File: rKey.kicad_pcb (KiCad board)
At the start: 2 copper layers, 54.4 x 78.7 mm, 35 parts, among them IC1 7805, J1 Conn_01x06, Q1 BC337, Q2 BC337, Q3 BC337, Q4 BC337, Q5 BC327, Q6 BC337, Q7 BC337, Q8 BC337, U1 TL084BCN, U2 TL084BCN

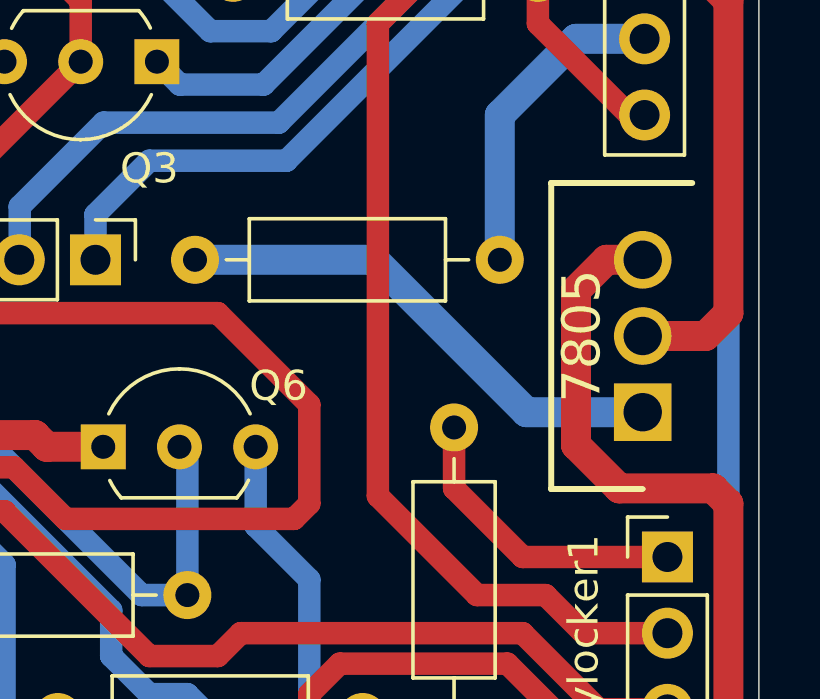
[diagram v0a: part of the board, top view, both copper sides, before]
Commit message: fix: 7805 wrong oriented
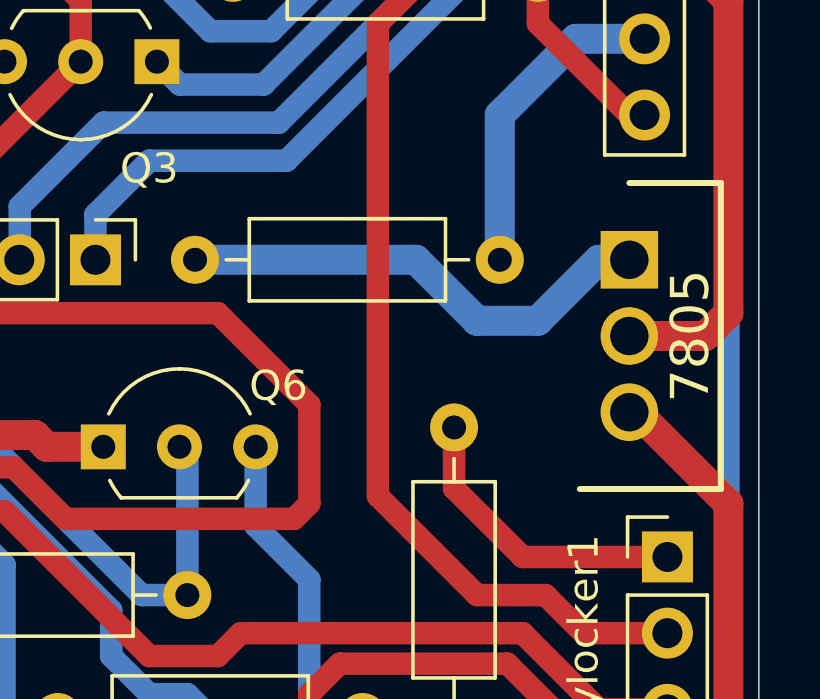
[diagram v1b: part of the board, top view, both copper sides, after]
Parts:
- moved IC1 5.10 mm to (165.1, 95.5), turned to -90 degrees
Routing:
- net Net-(C1-Pad1): track 48.4 -> 39.1 mm
- net Net-(IC1-Pad1): track 17.0 -> 16.2 mm
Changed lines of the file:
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@@
   )
   (footprint "KiCad:TO254P470X1000X1610-3P" (layer "F.Cu")
-    (at 165.546 100.584 90)
+    (at 165.1 95.504 -90)
     (descr "7805")
     (tags "Integrated Circuit")
@@
     (fp_line (start -2.56 -1.78) (end -1.29 -3.05) (layer "F.Fab") (width 0.1))
     (fp_line (start -2.56 -3.05) (end 7.64 -3.05) (layer "F.Fab") (width 0.1))
-    (pad "1" thru_hole rect locked (at 0 0 90) (size 1.92 1.92) (drill 1.28) (layers *.Cu *.Mask)
+    (pad "1" thru_hole rect locked (at 0 0 270) (size 1.92 1.92) (drill 1.28) (layers *.Cu *.Mask)
       (net 11 "Net-(IC1-Pad1)") (pinfunction "IN") (pintype "passive"))
-    (pad "2" thru_hole circle locked (at 2.54 0 90) (size 1.92 1.92) (drill 1.28) (layers *.Cu *.Mask)
+    (pad "2" thru_hole circle locked (at 2.54 0 270) (size 1.92 1.92) (drill 1.28) (layers *.Cu *.Mask)
       (net 4 "GND") (pinfunction "GND") (pintype "passive"))
-    (pad "3" thru_hole circle locked (at 5.08 0 90) (size 1.92 1.92) (drill 1.28) (layers *.Cu *.Mask)
+    (pad "3" thru_hole circle locked (at 5.08 0 270) (size 1.92 1.92) (drill 1.28) (layers *.Cu *.Mask)
       (net 43 "Net-(C1-Pad1)") (pinfunction "OUT") (pintype "passive"))
     (model "7805.stp"
@@
   (segment (start 137.145 95.504) (end 137.145 98.029) (width 0.75) (layer "B.Cu") (net 10))
   (segment (start 150.368 102.002) (end 150.368 106.68) (width 0.75) (layer "B.Cu") (net 10))
-  (segment (start 161.671 100.584) (end 165.546 100.584) (width 1) (layer "B.Cu") (net 11))
-  (segment (start 156.591 95.504) (end 161.671 100.584) (width 1) (layer "B.Cu") (net 11))
-  (segment (start 150.622 95.504) (end 156.591 95.504) (width 1) (layer "B.Cu") (net 11))
+  (segment (start 164.084 95.504) (end 165.1 95.504) (width 1) (layer "B.Cu") (net 11))
+  (segment (start 160.02 97.536) (end 162.052 97.536) (width 1) (layer "B.Cu") (net 11))
+  (segment (start 157.988 95.504) (end 160.02 97.536) (width 1) (layer "B.Cu") (net 11))
+  (segment (start 150.622 95.504) (end 157.988 95.504) (width 1) (layer "B.Cu") (net 11))
+  (segment (start 162.052 97.536) (end 164.084 95.504) (width 1) (layer "B.Cu") (net 11))
   (segment (start 160.782 90.678) (end 163.322 88.138) (width 1) (layer "B.Cu") (net 12))
   (segment (start 163.322 88.138) (end 165.608 88.138) (width 1) (layer "B.Cu") (net 12))
@@
   (segment (start 123.952 83.058) (end 124.714 82.296) (width 1) (layer "B.Cu") (net 41))
   (segment (start 124.714 82.296) (end 124.714 77.851) (width 1) (layer "B.Cu") (net 41))
-  (segment (start 164.338 95.504) (end 165.738405 95.504) (width 1) (layer "F.Cu") (net 43))
-  (segment (start 163.322 96.52) (end 164.338 95.504) (width 1) (layer "F.Cu") (net 43))
-  (segment (start 163.322 101.68) (end 163.322 96.52) (width 1) (layer "F.Cu") (net 43))
-  (segment (start 168.402 103.632) (end 167.894 103.124) (width 1) (layer "F.Cu") (net 43))
+  (segment (start 168.402 122.428) (end 168.402 103.632) (width 1) (layer "F.Cu") (net 43))
+  (segment (start 165.354 100.584) (end 165.1 100.584) (width 1) (layer "F.Cu") (net 43))
+  (segment (start 167.64 123.19) (end 168.402 122.428) (width 1) (layer "F.Cu") (net 43))
   (segment (start 166.37 123.19) (end 167.64 123.19) (width 1) (layer "F.Cu") (net 43))
-  (segment (start 167.894 103.124) (end 164.766 103.124) (width 1) (layer "F.Cu") (net 43))
-  (segment (start 168.402 122.428) (end 168.402 103.632) (width 1) (layer "F.Cu") (net 43))
-  (segment (start 167.64 123.19) (end 168.402 122.428) (width 1) (layer "F.Cu") (net 43))
-  (segment (start 164.766 103.124) (end 163.322 101.68) (width 1) (layer "F.Cu") (net 43))
+  (segment (start 168.402 103.632) (end 165.354 100.584) (width 1) (layer "F.Cu") (net 43))
   (segment (start 160.02 115.316) (end 161.036 116.332) (width 1) (layer "B.Cu") (net 43))
   (segment (start 164.084 123.19) (end 166.37 123.19) (width 1) (layer "B.Cu") (net 43))

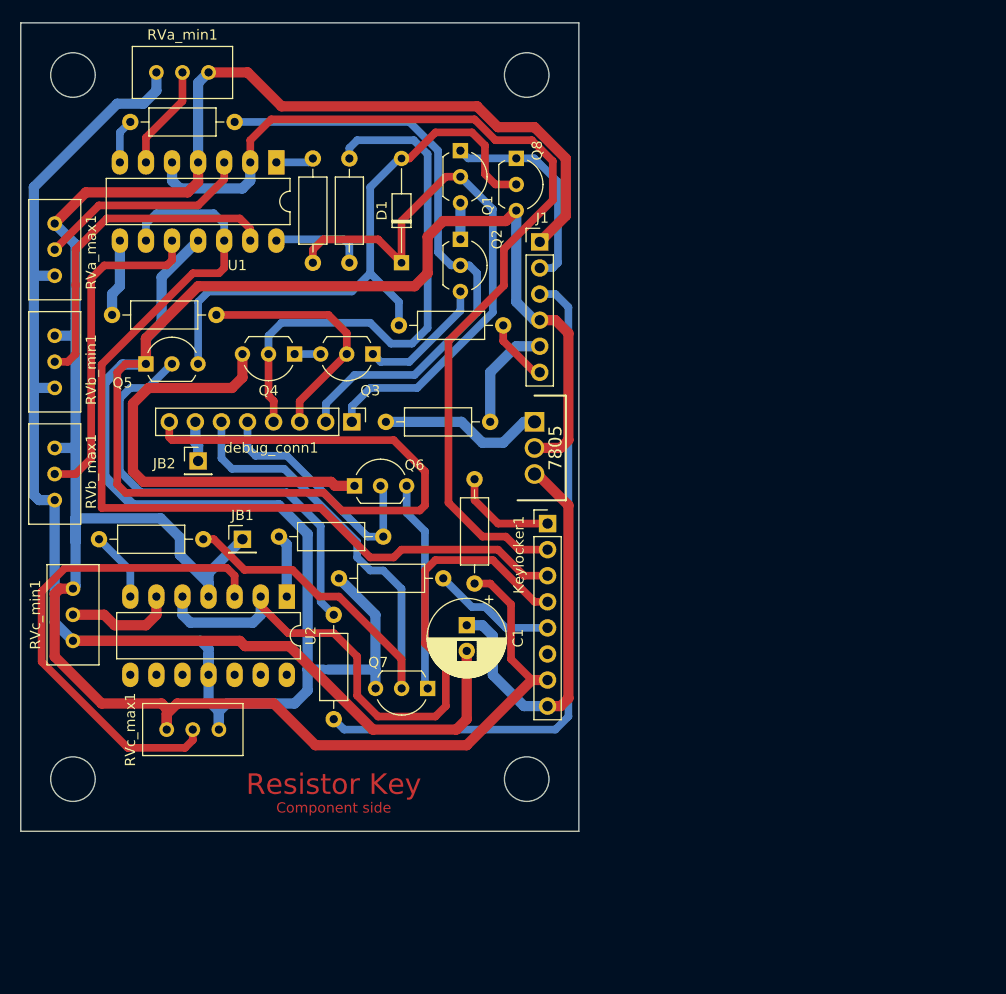
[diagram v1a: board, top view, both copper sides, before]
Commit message: fix: small changes in footprint associations
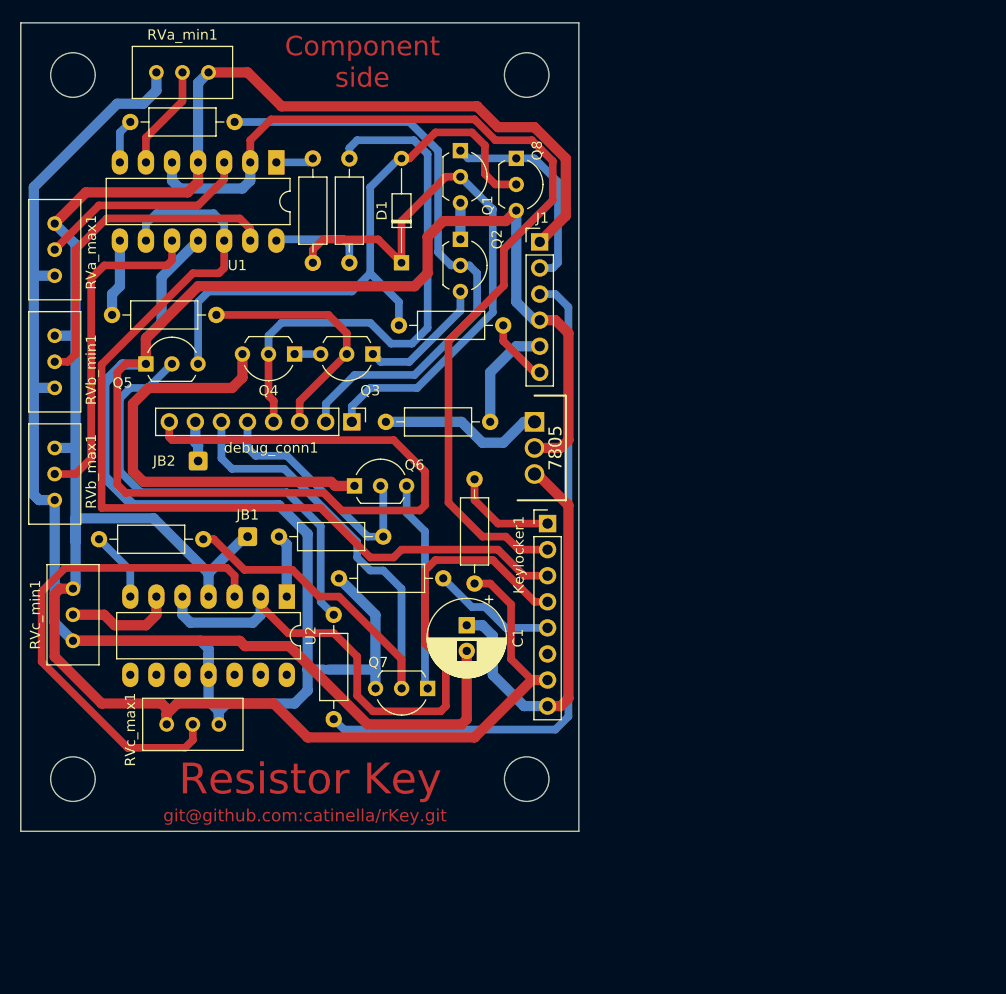
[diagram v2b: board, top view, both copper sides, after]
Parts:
- JB1, JB2: footprint Connector_PinHeader_2.54mm:PinHeader_1x01_P2.54mm_Vertical -> Connector_Wire:SolderWire-0.25sqmm_1x01_D0.65mm_OD1.7mm
- moved JB1 0.57 mm to (137.2, 106.7)
- moved RVc_max1 0.51 mm to (129.3, 125.0)
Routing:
- net Net-(J1-Pad1): track 219.9 -> 216.7 mm
- net GND: track 387.2 -> 385.7 mm
- net Net-(RVc_max1-Pad2): track 48.5 -> 49.0 mm
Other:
- board text added: "git@github.com:catinella/rKey.git"

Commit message: Preliminary version
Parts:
- removed JB1, JB2: Conn_01x01, Connector_Wire:SolderWire-0.25sqmm_1x01_D0.65mm_OD1.7mm
- added R11: 100K, Resistor_THT:R_Axial_DIN0207_L6.3mm_D2.5mm_P10.16mm_Horizontal, F.Cu at (128.8, 103.1)
- added R12: 100K, Resistor_THT:R_Axial_DIN0207_L6.3mm_D2.5mm_P10.16mm_Horizontal, F.Cu at (128.8, 106.4)
- added R14: 100K, Resistor_THT:R_Axial_DIN0207_L6.3mm_D2.5mm_P10.16mm_Horizontal, F.Cu at (128.8, 99.8)
- added R15: 100K, Resistor_THT:R_Axial_DIN0207_L6.3mm_D2.5mm_P10.16mm_Horizontal, F.Cu at (151.6, 99.8)
- added R16: 100K, Resistor_THT:R_Axial_DIN0207_L6.3mm_D2.5mm_P10.16mm_Horizontal, F.Cu at (151.6, 106.4)
- added R17: 100K, Resistor_THT:R_Axial_DIN0207_L6.3mm_D2.5mm_P10.16mm_Horizontal, F.Cu at (151.6, 103.1)
- moved C1 45.0 mm to (202.9, 108.1)
- moved R13 21.6 mm to (124.0, 114.0)
- moved R10 20.4 mm to (145.3, 128.0)
- moved RVc_max1 14.2 mm to (118.4, 115.8), turned to 90 degrees
- moved Q7 12.5 mm to (155.8, 109.0), turned to -90 degrees
- moved Q6 8.09 mm to (155.6, 101.3), turned to -90 degrees
- moved RVc_min1 7.82 mm to (118.4, 104.1)
- moved R8 6.76 mm to (128.3, 110.7)
- moved RVa_max1 5.32 mm to (118.4, 70.9)
- moved RVb_min1 5.32 mm to (118.4, 81.8)
- moved RVb_max1 5.08 mm to (118.4, 93.0)
- moved R7 5.00 mm to (142.2, 111.3)
- moved U2 4.20 mm to (142.7, 116.3)
- moved R1 2.87 mm to (161.3, 109.2)
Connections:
- debug_conn1 pad 7: Net-(JB2-Pad1) -> Net-(J1-Pad1)
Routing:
- net GND: track 385.7 -> 249.0 mm
- net Net-(Keylocker1-Pad3): track 91.0 -> 30.3 mm
- net Net-(Q6-Pad2): track 24.4 -> 52.0 mm
- net Net-(RVc_max1-Pad2): track 49.0 -> 23.9 mm
- net Net-(J1-Pad3): track 67.0 -> 43.2 mm
- net Net-(Keylocker1-Pad4): track 65.5 -> 42.2 mm
- net Net-(Q7-Pad2): track 64.0 -> 42.9 mm
- net Net-(Q4-Pad3): track 42.8 -> 63.0 mm
- net Net-(Q6-Pad3): track 20.6 -> 2.60 mm
- net Net-(Q3-Pad2): track 24.0 -> 40.9 mm
- net Net-(Q5-Pad2): track 44.5 -> 27.6 mm
- net Net-(Q4-Pad2): track 52.5 -> 68.9 mm
- net Net-(C1-Pad1): track 39.1 -> 23.4 mm
- net Net-(J1-Pad1): track 216.7 -> 231.1 mm
- net Net-(Keylocker1-Pad5): track 12.2 -> 0.00 mm
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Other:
- outline, holes or cut-outs redrawn

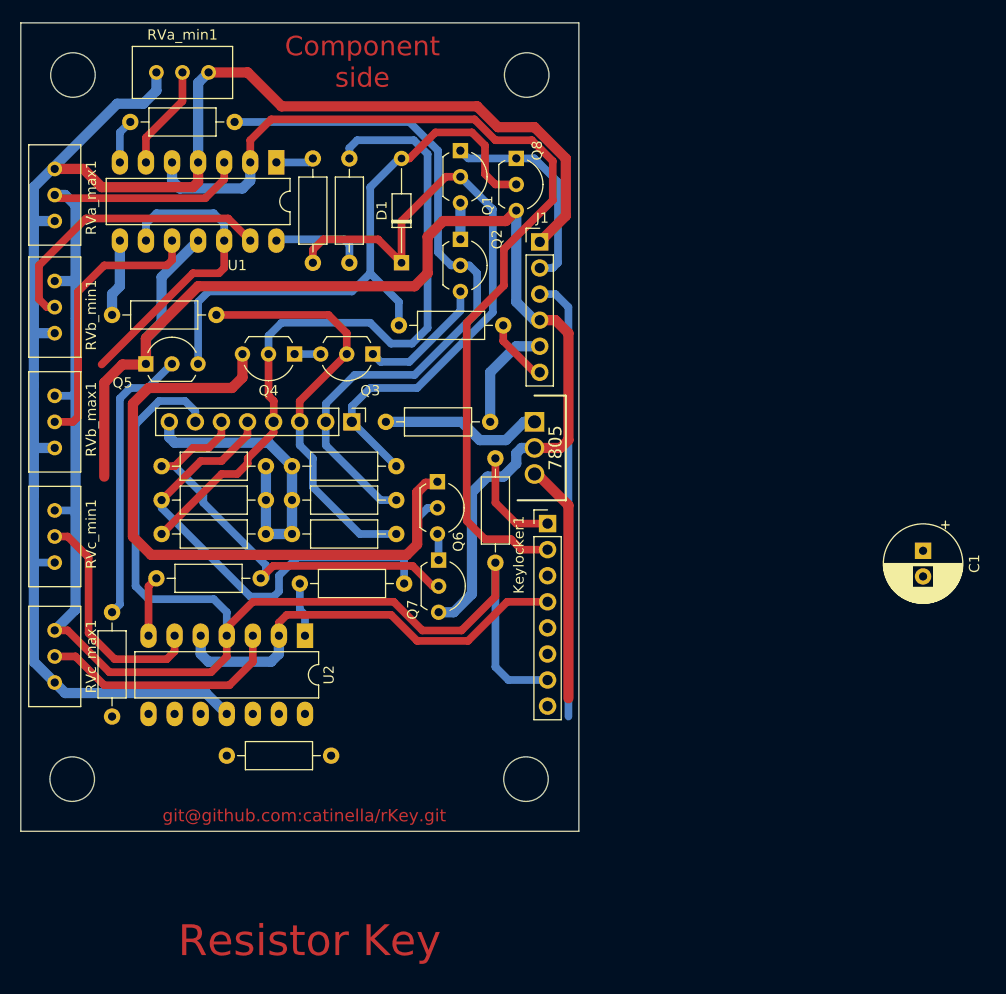
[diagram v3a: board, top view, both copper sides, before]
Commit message: fix: PULL-UP resistors added
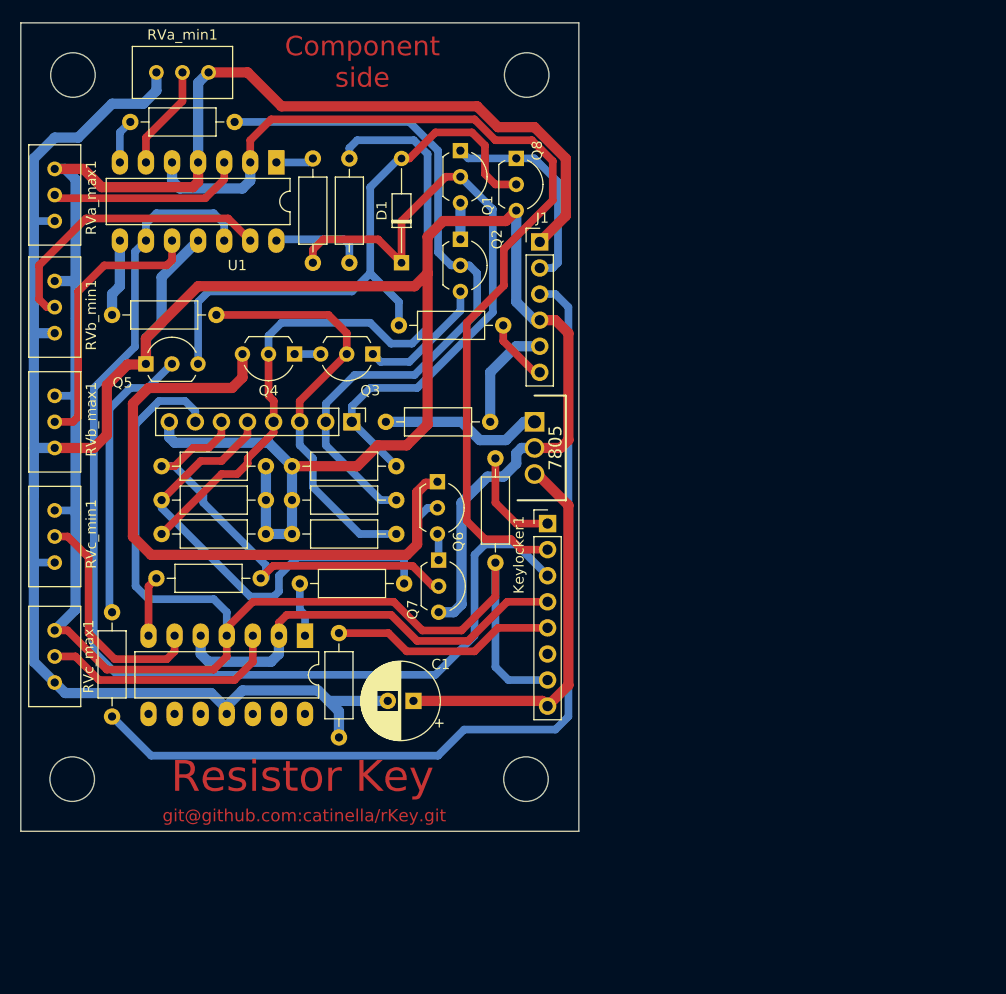
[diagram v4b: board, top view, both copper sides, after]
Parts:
- moved C1 51.7 mm to (153.3, 122.7), turned to 180 degrees
- moved R10 12.0 mm to (146.1, 116.1), turned to -90 degrees
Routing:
- net Net-(Keylocker1-Pad3): track 30.3 -> 110.2 mm
- net GND: track 249.0 -> 304.6 mm
- net Net-(J1-Pad3): track 43.2 -> 90.8 mm
- net Net-(Keylocker1-Pad5): track 0.00 -> 22.0 mm
- net Net-(C1-Pad1): track 23.4 -> 38.2 mm
- net Net-(J1-Pad1): track 231.1 -> 233.4 mm
